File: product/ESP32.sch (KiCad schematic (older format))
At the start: 26 parts, among them J1 10118192-0001LF, J2 Conn_02x05_Odd_Even, Q1 Q_NMOS_GSD, Q2 Q_NMOS_GSD, Q3 Q_NMOS_GSD, SW1 PTS645VH83-2 LFS, U1 AZ1117EH-3.3, U3 ESP32-WROOM-32D

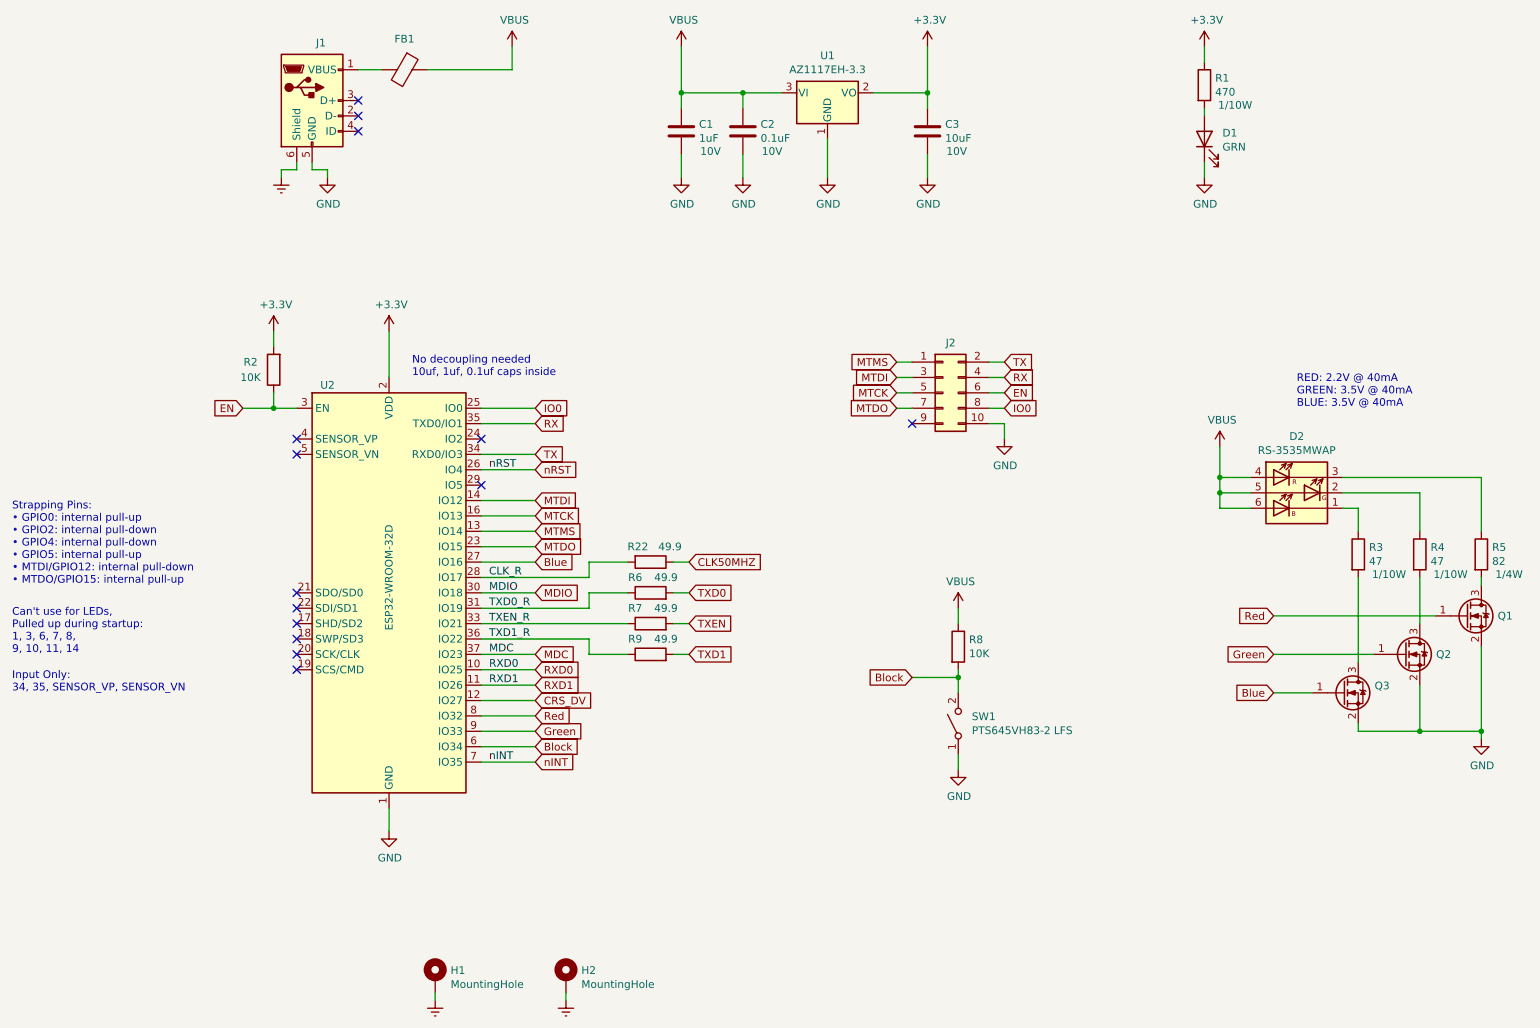
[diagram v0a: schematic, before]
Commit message: Added LCSC part numbers, and tweaked a few part footprints
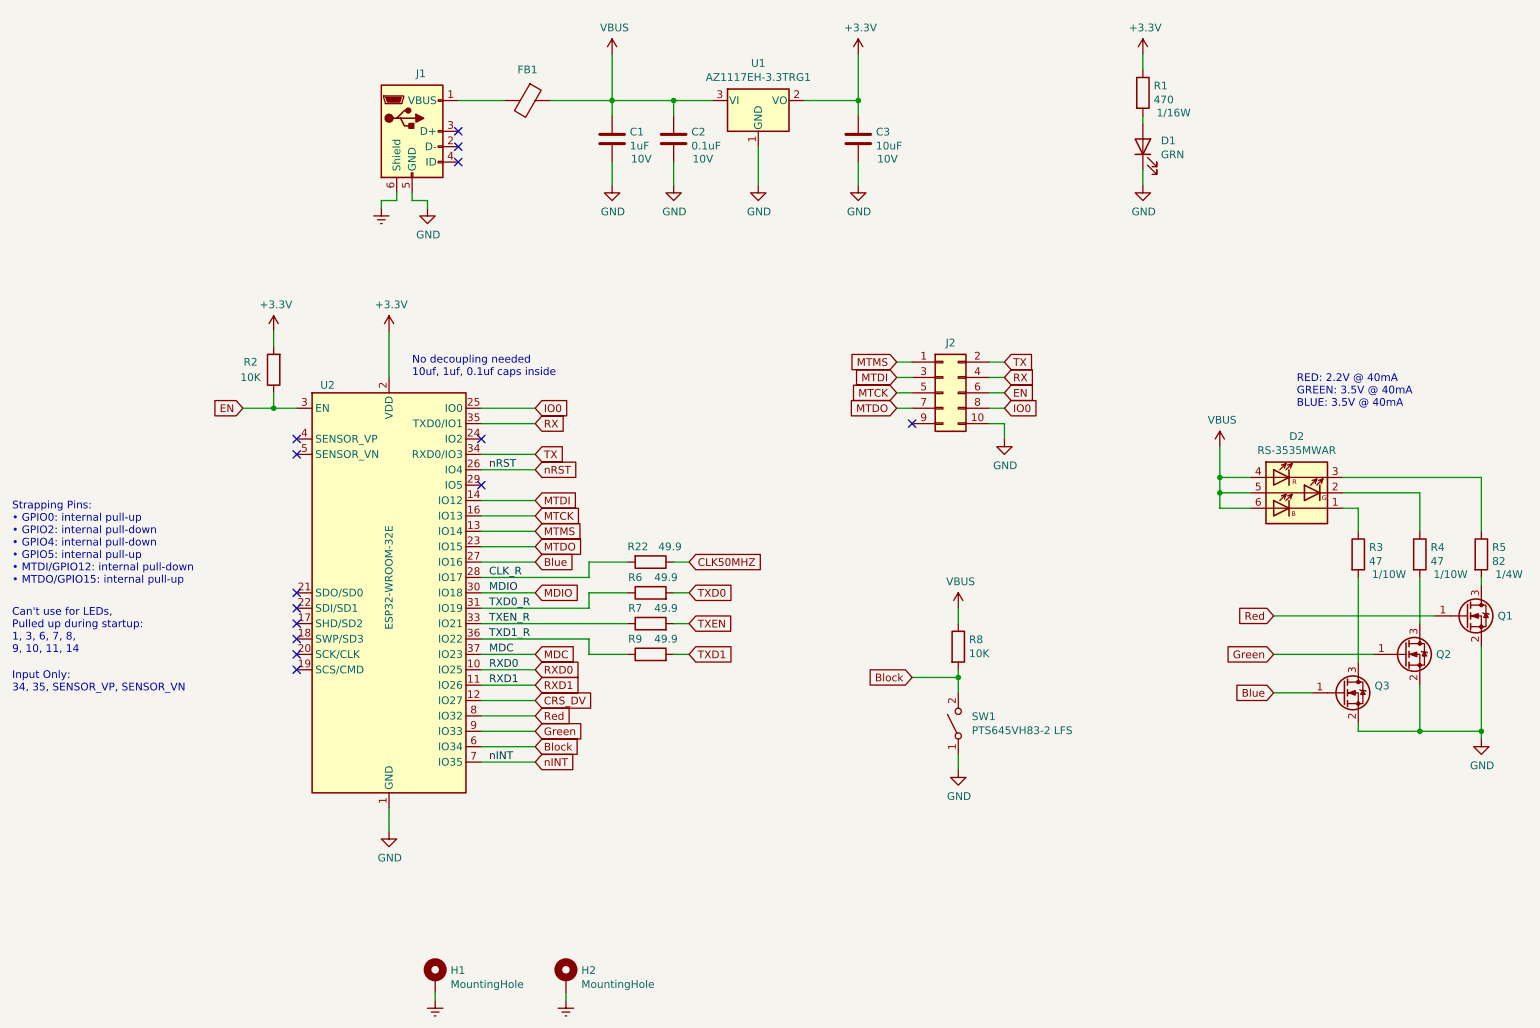
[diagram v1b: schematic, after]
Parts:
- C1: LCSC (none) -> C52923; LCSC Part Number (none) -> C52923
- C2: LCSC (none) -> C1525; LCSC Part Number (none) -> C1525
- C3: footprint Capacitor_SMD:C_0603_1608Metric -> Capacitor_SMD:C_0805_2012Metric; LCSC (none) -> C19702; LCSC Part Number (none) -> C19702
- D1: LCSC (none) -> C72043; LCSC Part Number (none) -> C72043
- D2: value RS-3535MWAP -> RS-3535MWAR; LCSC (none) -> C110402; LCSC Part Number (none) -> C110402
- FB1: footprint Inductor_SMD:L_0603_1608Metric -> Inductor_SMD:L_0805_2012Metric; LCSC (none) -> C1015; LCSC Part Number (none) -> C1015
- Q1, Q2, Q3: value Q_NMOS_GSD -> 2N7002; LCSC (none) -> C8545; LCSC Part Number (none) -> C8545
- R1: LCSC (none) -> C270656; LCSC Part Number (none) -> C270656; Rating 1/10W -> 1/16W
- R2, R8: LCSC (none) -> C25744; LCSC Part Number (none) -> C25744
- R22, R6, R7, R9: LCSC (none) -> C25120; LCSC Part Number (none) -> C25120
- R3, R4: LCSC (none) -> C23182; LCSC Part Number (none) -> C23182
- R5: LCSC (none) -> C247183; LCSC Part Number (none) -> C247183; LCSC# C247183 -> (none)
- U1: value AZ1117EH-3.3 -> AZ1117EH-3.3TRG1; Extended Part (none) -> X; LCSC (none) -> C108494; LCSC Part Number (none) -> C108494
- U3: value ESP32-WROOM-32D -> ESP32-WROOM-32E; Extended Part (none) -> X; LCSC (none) -> C52923; LCSC Part Number (none) -> C701341
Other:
- moved on the sheet: C1, C2, C3, D1, FB1, J1, R1, U1
